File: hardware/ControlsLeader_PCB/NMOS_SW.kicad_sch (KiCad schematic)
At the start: 7 parts, among them Q1 NMOS

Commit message: ShaqDash is born. . . RPP in progress
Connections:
- net 3.3V_Switch_Signal renamed 5V_Switch_Signal
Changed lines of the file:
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@@
 		)
 	)
-	(hierarchical_label "3.3V_Switch_Signal"
+	(hierarchical_label "5V_Switch_Signal"
 		(shape input)
 		(at 118.11 100.33 180)
@@
 		(dnp no)
 		(property "Reference" "D1"
-			(at 137.16 104.4574 90)
-			(effects
-				(font
+			(at 134.874 104.394 90)
+			(effects
+				(font

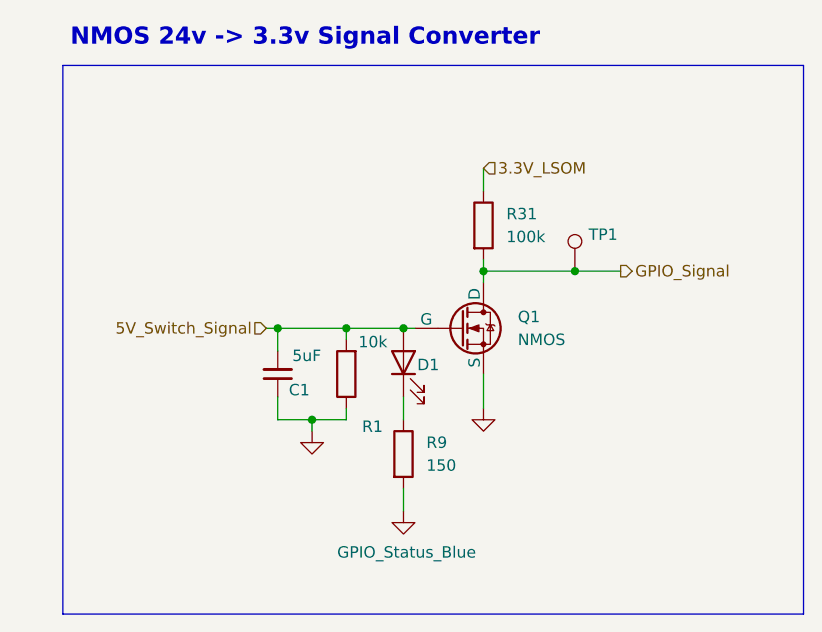
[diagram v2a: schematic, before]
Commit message: updated jlc parts list
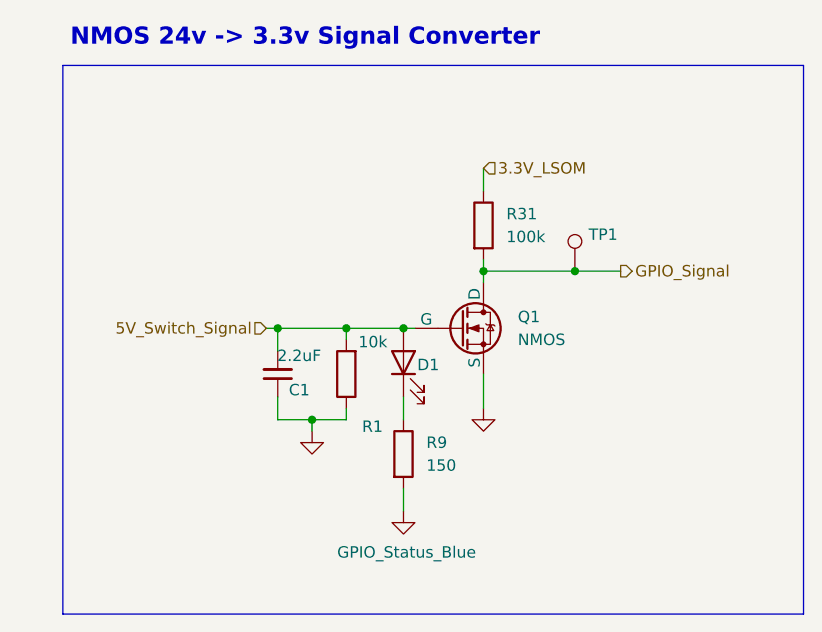
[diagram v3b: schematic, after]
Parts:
- C1: value 5uF -> 2.2uF
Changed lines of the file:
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@@
 			)
 		)
-		(property "Value" "5uF"
+		(property "Value" "2.2uF"
 			(at 124.206 103.378 0)
 			(effects
